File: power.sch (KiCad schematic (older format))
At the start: 28 parts, among them J91 AUX/SYS PWR, J92 AUX PWR, U91 stm795, U92 TPS3808, U93 LM1117-1.2, U94 LM1117-2.5, U95 LM1117-3.3, X96 SIT1602BC-23-25N-48.000000

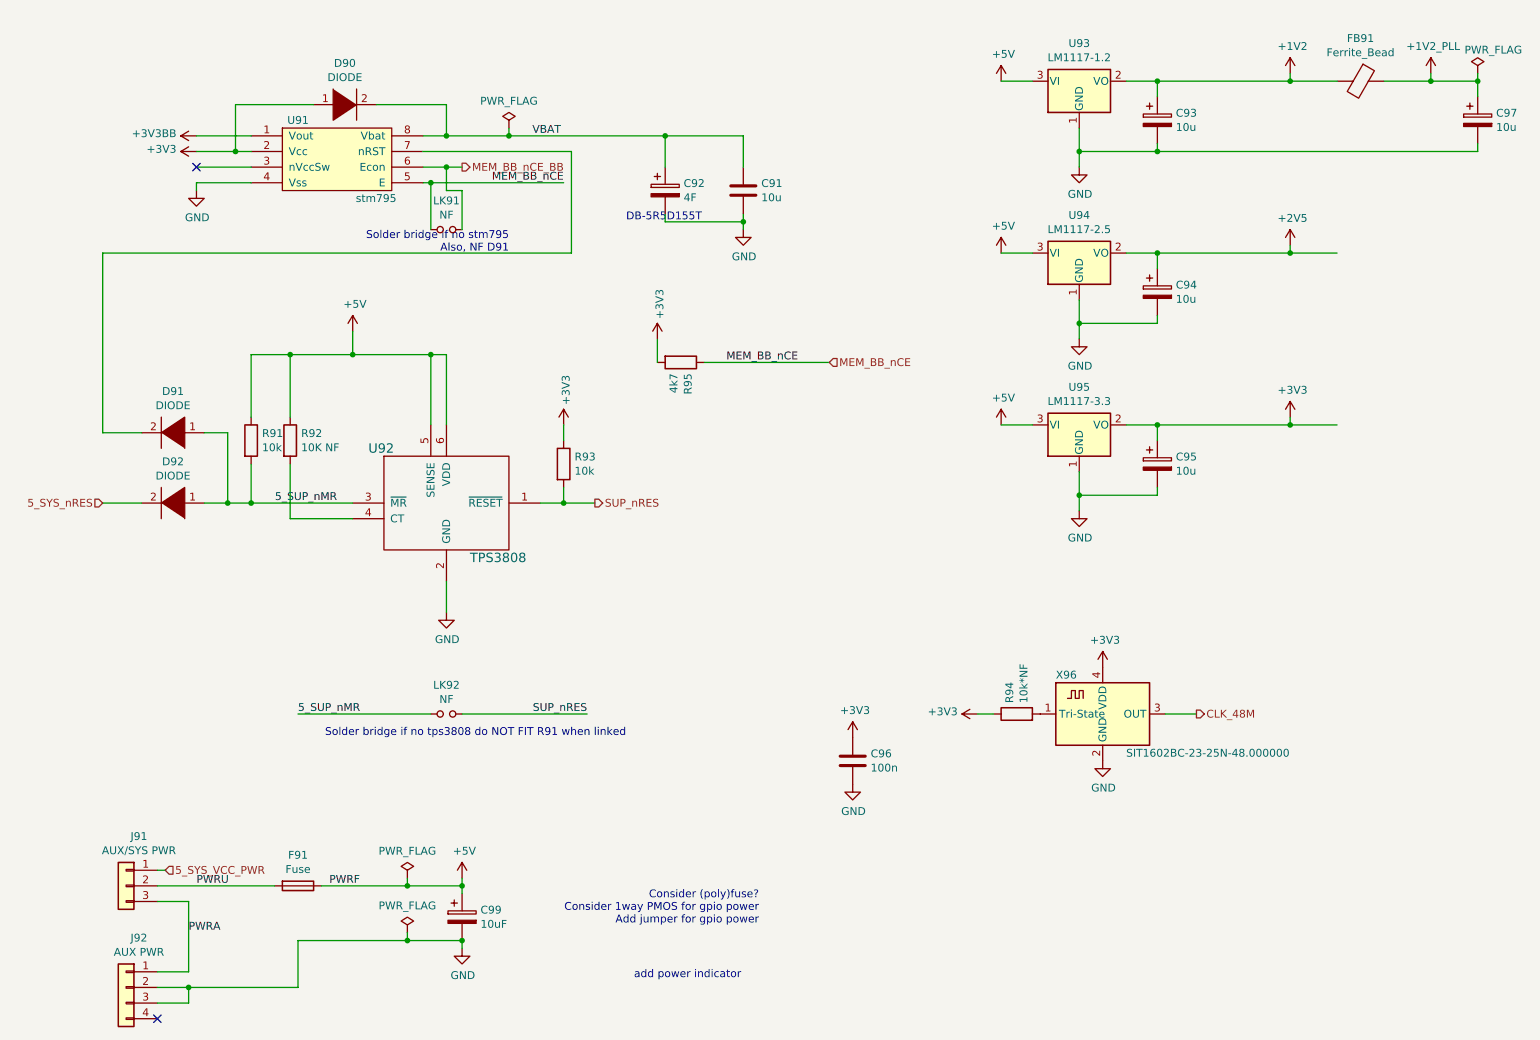
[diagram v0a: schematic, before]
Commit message: Mk.3 fixes and new 68000 expansion board
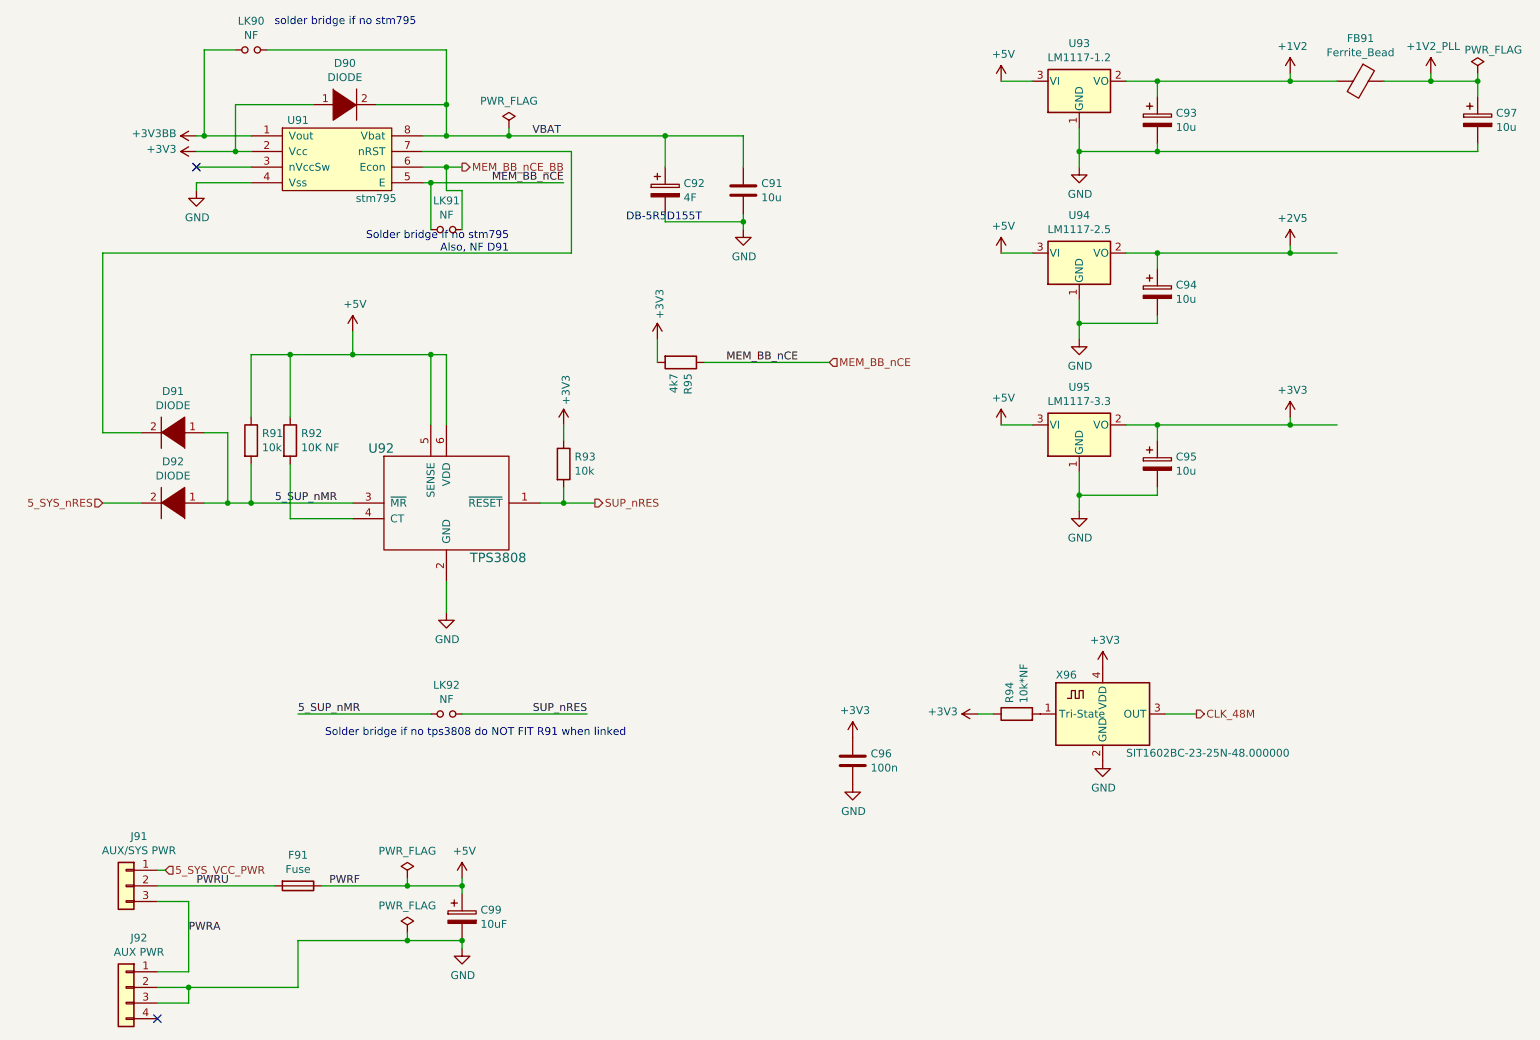
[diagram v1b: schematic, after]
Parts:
- added LK90: NF, mk3blit:SolderJumper-2_P1.3mm_Open_RoundedPad1.0x1.5mm-domsmallctyd, symbol Device:Jumper_NO_Small
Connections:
- net +3V3BB: now also LK90.1
- net VBAT: now also LK90.2
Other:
- note added: "solder bridge if no stm795"
- note removed: "Consider (poly)fuse?\nConsider 1way PMOS for gpio power\nAdd jumper for gpio power"
- note removed: "add power indicator"
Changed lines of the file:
@@
 Sheet 4 11
 Title "Mk.3 Blitter FPGA development board"
-Date "2021-05-08"
-Rev "3.00"
+Date "2021-08-14"
+Rev "3.03"
 Comp "Dossytronics"
-Comment1 ""
+Comment1 "fixed: clk/sysd0, jtag, u22 footprint"
 Comment2 ""
 Comment3 ""
@@
 Wire Wire Line
 	3450 6750 3450 6700
-Text Notes 5350 6600 2    50   ~ 0
-Consider (poly)fuse?\nConsider 1way PMOS for gpio power\nAdd jumper for gpio power
 $Comp
 L Connector_Generic:Conn_01x04 J92
@@
 	7900 1200 8750 1200
 Wire Wire Line
-	1750 1550 2100 1550
+	1750 1550 1800 1550
 Text HLabel 1150 3900 0    50   Input ~ 0
 5_SYS_nRES
@@
 Wire Wire Line
 	3350 1750 3450 1750
-Text Notes 4550 6950 0    50   ~ 0
-add power indicator
 $Comp
 L Device:CP C92
@@
 	9950 1300 9950 1200
 Connection ~ 9950 1200
+$Comp
+L Device:Jumper_NO_Small LK90
+U 1 1 61239010
+P 2100 1000
+F 0 "LK90" H 2100 1185 50  0000 C CNN
+F 1 "NF" H 2100 1094 50  0000 C CNN
+F 2 "mk3blit:SolderJumper-2_P1.3mm_Open_RoundedPad1.0x1.5mm-domsmallctyd" H 2100 1000 50  0001 C CNN
+F 3 "~" H 2100 1000 50  0001 C CNN
+	1    2100 1000
+	1    0    0    -1
+$EndComp
+Wire Wire Line
+	2200 1000 3350 1000
+Wire Wire Line
+	3350 1000 3350 1350
+Connection ~ 3350 1350
+Wire Wire Line
+	2000 1000 1800 1000
+Wire Wire Line
+	1800 1000 1800 1550
+Connection ~ 1800 1550
+Wire Wire Line
+	1800 1550 2100 1550
+Text Notes 2250 850  0    50   ~ 0
+solder bridge if no stm795
 $EndSCHEMATC

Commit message: Updates from SVN to rev3.03
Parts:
- C99: value 10uF -> 10u
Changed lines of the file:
@@
 EESchema Schematic File Version 4
-LIBS:blit-cpu-mk3-cache
-EELAYER 29 0
+EELAYER 30 0
 EELAYER END
 $Descr A4 11693 8268
@@
 P 3450 6550
 F 0 "C99" H 3568 6596 50  0000 L CNN
-F 1 "10uF" H 3568 6505 50  0000 L CNN
+F 1 "10u" H 3568 6505 50  0000 L CNN
 F 2 "Capacitors_SMD:C_0805" H 3488 6400 50  0001 C CNN
 F 3 "~" H 3450 6550 50  0001 C CNN
